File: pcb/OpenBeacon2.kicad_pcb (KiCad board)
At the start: 2 copper layers, 100 x 80 mm, 87 parts, among them J1 Bias V, J10 UART, J11 BNC, J2 PAI+, J3 PAI-, J4 Digital IO, J5 ADC Inputs, J6 SMA, J8 I2C Bus, J9 GND, K1 G5V-1-DC5, K2 G5V-1-DC5, M1 LPF 1, M2 LPF 2, Q1 2N7002, Q2 MMBT4403, Q3 2SK3074, Q4 2N7002, Q5 2N7002, Q6 2N7002, U1 TLV61046A, U2 ASTX-H11-25.000MHZ-T, U3 SN74LVC1G17, U4 SI5351A, U5 MCP4725A1T-E/CH, U6 128x32 OLED, U7 Empyrean, U8 24AA64T

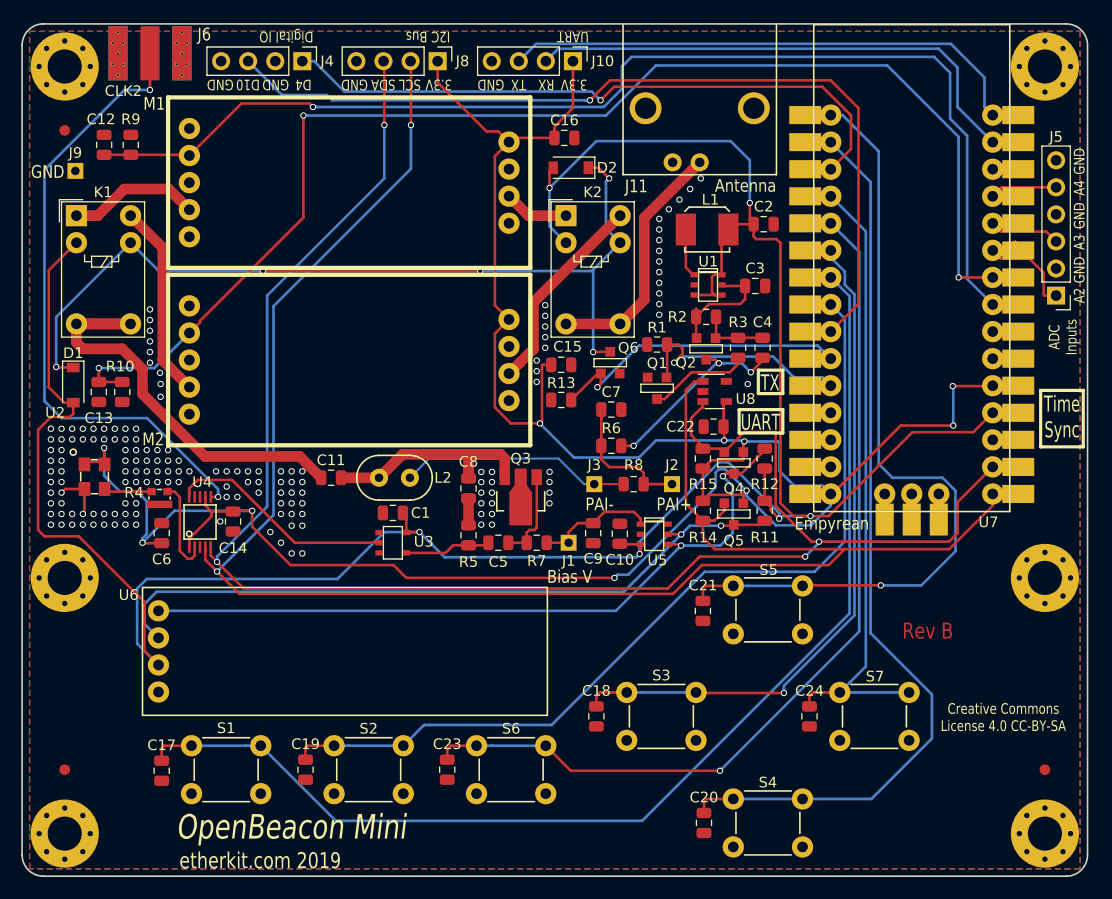
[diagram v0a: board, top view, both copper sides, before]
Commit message: Fix fw where freq would show as 0 during startup
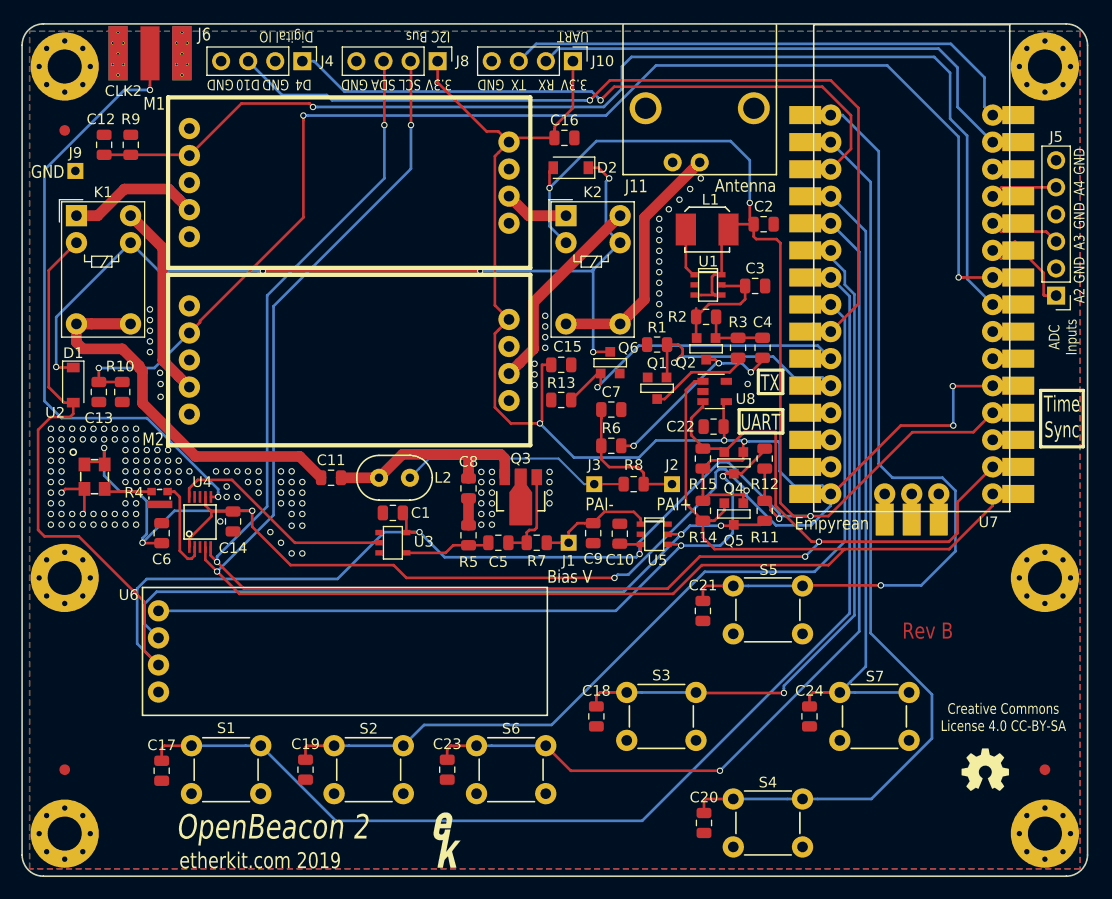
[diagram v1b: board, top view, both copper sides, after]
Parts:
- added G***: LOGO, EtherkitKicadLibrary:OSHWLogo4mm, F.Cu at (190.4, 120.0)
- added Ref**: Val**, EtherkitKicadLibrary:EtherkitLogoSmall, F.Cu at (139.9, 126.6)
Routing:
- net Net-(C11-Pad1): track 41.5 -> 42.0 mm
- net GND: vias 155 -> 151
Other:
- board text added: "OpenBeacon 2"
- board text removed: "OpenBeacon Mini"
